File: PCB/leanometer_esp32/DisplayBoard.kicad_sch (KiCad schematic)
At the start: 26 parts, among them J6 Conn_01x07, Q1 BSS138, U4 74HC595, U6 74HC595, U6 D168K, U7 D168K

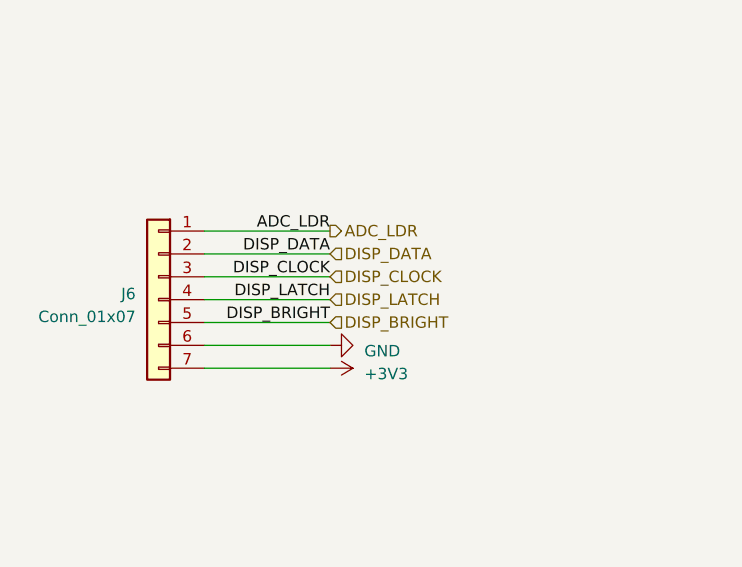
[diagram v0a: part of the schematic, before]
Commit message: Added PowerBoard hierarchical sheet, completed layout
Signed-off-by: theloukou
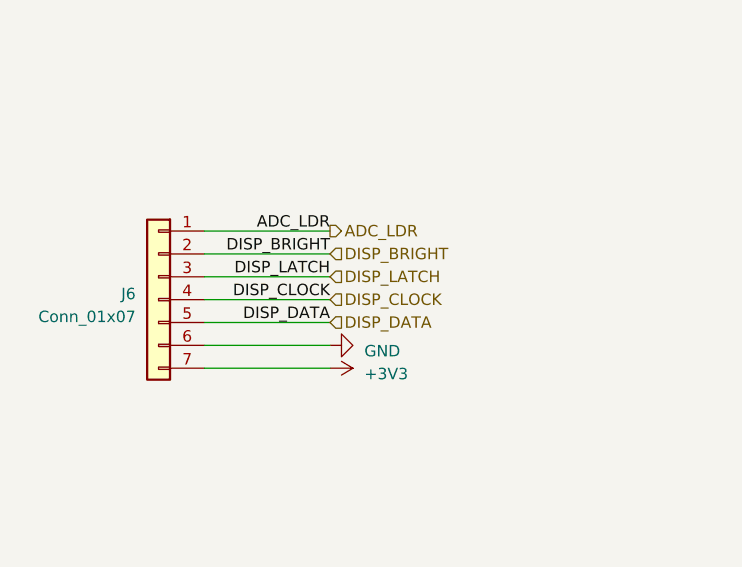
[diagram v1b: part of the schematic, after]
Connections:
- net DISP_BRIGHT: now also J6.2 (Pin_2); no longer J6.5 (Pin_5)
- net DISP_CLOCK: now also J6.4 (Pin_4); no longer J6.3 (Pin_3)
- net DISP_DATA: now also J6.5 (Pin_5); no longer J6.2 (Pin_2)
- net DISP_LATCH: now also J6.3 (Pin_3); no longer J6.4 (Pin_4)
